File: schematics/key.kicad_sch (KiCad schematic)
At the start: 6 parts, among them Q1 SS8050, Q2 IRLML5203

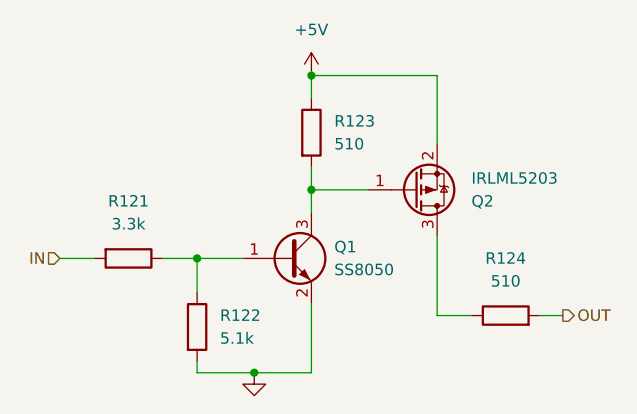
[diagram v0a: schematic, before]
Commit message: Обновил схемотехнику у платы. Убрал лишнее компоненты и лишнии линии
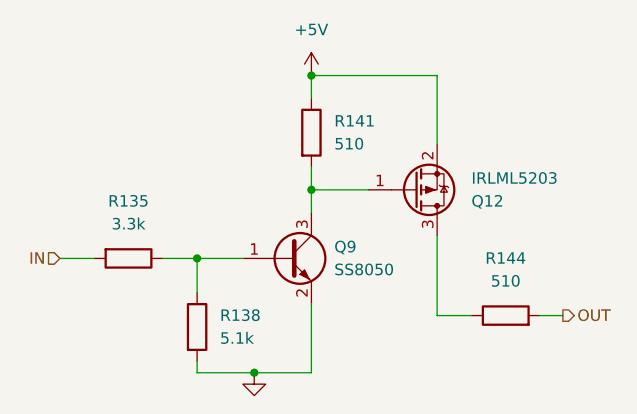
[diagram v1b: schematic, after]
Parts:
- renumbered Q2 to Q12, Q1 to Q9, R121 to R135, R122 to R138, R123 to R141, R124 to R144
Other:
- company: (none) -> МГТУ им. Н.Э.Баумана

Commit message: Обновлена нумерация элементов
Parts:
- renumbered Q9 to Q1, Q12 to Q2, R135 to R20, R138 to R21, R141 to R22, R144 to R23
